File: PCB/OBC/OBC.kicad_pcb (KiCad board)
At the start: 4 copper layers, 81 x 81 mm, 130 parts, among them IC1 TPS2553QDBVRQ1, J2 Conn_02x24_Odd_Even, J3 USB_C_Receptacle_USB2.0_16P, U1 STM32F405RGTx, U10 TMUX1574PWR, U11 W25Q128JVSIQ, U12 SN65HVD230DR, U2 SN65HVD230DR, U3 USBLC6-2SC6, U4 STM32F405RGTx, U5 STM32F405RGTx, U6 MAX6369KA+T, U7 AMS1117-3.3, U8 TMUX1574PWR, U9 W25Q128JVSIQ

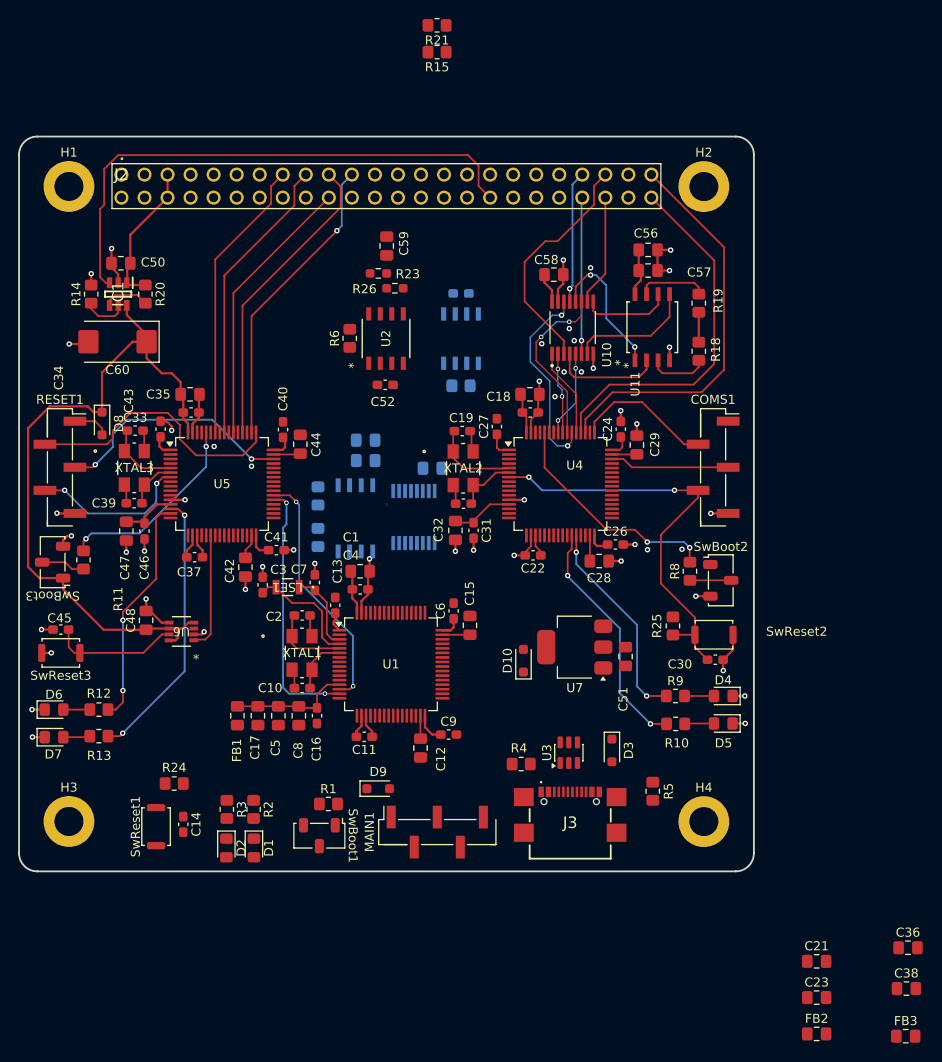
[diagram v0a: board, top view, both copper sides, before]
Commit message: Solo falta verificar el LDO
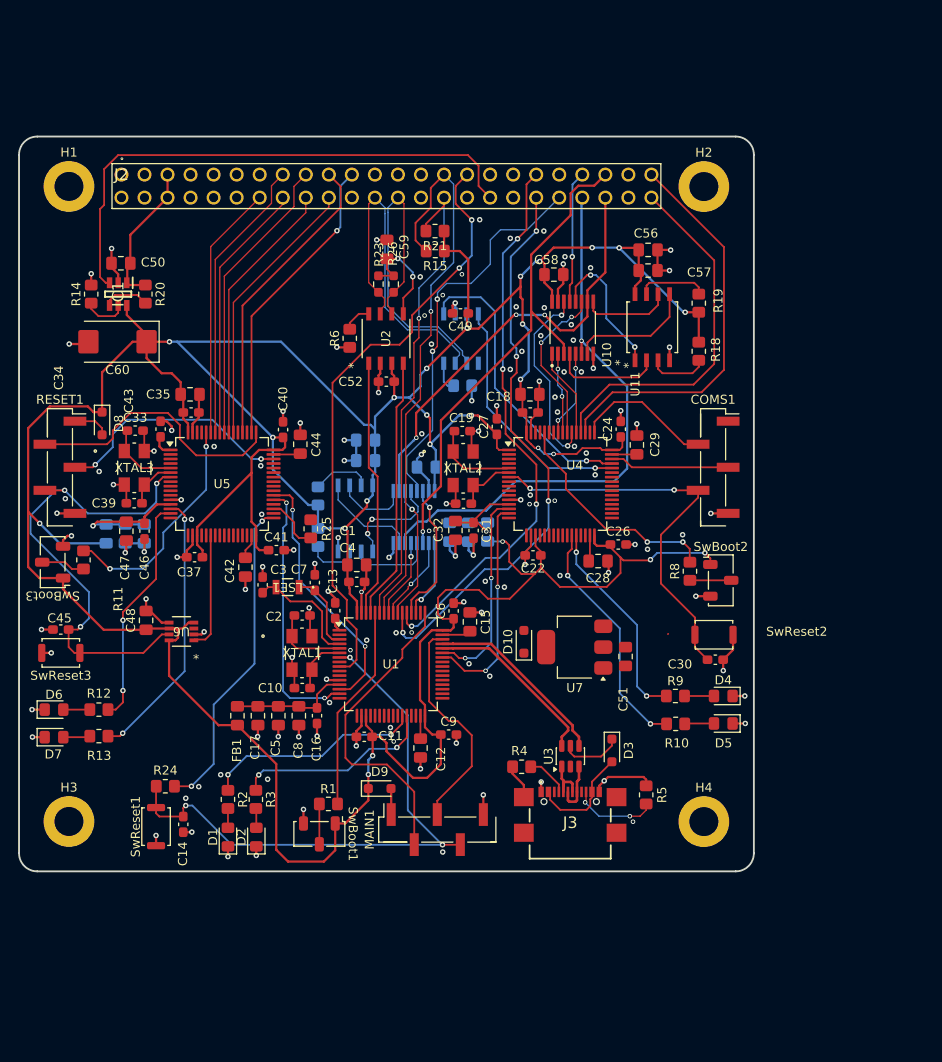
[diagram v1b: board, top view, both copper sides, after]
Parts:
- C21, C23, C36, C38, FB2, FB3: moved to B.Cu
- C49: moved to F.Cu
- moved FB3 104.1 mm to (119.5, 87.9), turned to 90 degrees
- moved C38 99.6 mm to (121.6, 87.9), turned to 90 degrees
- moved C36 95.8 mm to (123.7, 87.9), turned to 90 degrees
- moved FB2 66.2 mm to (161.6, 87.7), turned to 90 degrees
- moved C23 65.3 mm to (157.4, 87.7), turned to 90 degrees
- moved C21 60.9 mm to (159.4, 87.7), turned to 90 degrees
- moved R25 41.3 mm to (142.1, 87.3), turned to -90 degrees
- moved R21 22.7 mm to (155.8, 54.5)
- moved R15 21.9 mm to (155.8, 56.7)
- moved D2 3.51 mm to (136.1, 121.3), turned to 90 degrees
- moved R3 3.38 mm to (136.0, 117.2)
- moved D1 3.11 mm to (132.9, 121.3), turned to 90 degrees
- moved R2 3.03 mm to (132.9, 117.2)
- moved C49 2.20 mm to (158.6, 63.6)
- moved D10 2.09 mm to (165.6, 99.8)
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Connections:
- net CAN_H renamed CAN+
- net CAN_L renamed CAN-
- C16 pad 1: +3V3A -> +3V3AM
- C17 pad 1: +3V3A -> +3V3AM
- C21 pad 2: +3V3A -> +3V3AC
- C23 pad 2: +3V3A -> +3V3AC
- C31 pad 1: +3V3A -> +3V3AC
- C32 pad 1: +3V3A -> +3V3AC
- C36 pad 2: +3V3A -> +3V3AP
- C38 pad 2: +3V3A -> +3V3AP
- C46 pad 1: +3V3A -> +3V3AP
- C47 pad 1: +3V3A -> +3V3AP
- C5 pad 2: +3V3A -> +3V3AM
- C8 pad 2: +3V3A -> +3V3AM
- FB1 pad 2: +3V3A -> +3V3AM
- FB2 pad 2: +3V3A -> +3V3AC
- FB3 pad 2: +3V3A -> +3V3AP
- U1 pad 13: +3V3A -> +3V3AM
- U1 pad 37: SW2 -> unconnected-(U1-PC6-Pad37)
- U1 pad 38: SW1 -> unconnected-(U1-PC7-Pad38)
- U1 pad 40: EN_QUEMADOR -> unconnected-(U1-PC9-Pad40)
- U1 pad 50: CsMemPY -> unconnected-(U1-PA15-Pad50)
- U4 pad 13: +3V3A -> +3V3AC
- U5 pad 13: +3V3A -> +3V3AP
- U5 pad 55: unconnected-(U5-PB3-Pad55) -> EN_QUEMADOR
- U5 pad 57: unconnected-(U5-PB5-Pad57) -> SW2
- U5 pad 59: unconnected-(U5-PB7-Pad59) -> SW1
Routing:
- net +3V3: track 130.6 -> 484.3 mm, vias 0 -> 25
- net GND: track 105.4 -> 179.9 mm, vias 39 -> 133
- net Interrupción EPS: track 0.00 -> 66.3 mm, vias 0 -> 2
- net /Main/SWNRST: track 0.00 -> 65.6 mm, vias 0 -> 3
- net PY2_RX: track 0.00 -> 63.5 mm, vias 0 -> 4
- net I2C_SCL: track 0.00 -> 62.1 mm, vias 0 -> 1
- net PY2_TX: track 0.00 -> 61.6 mm, vias 0 -> 4
- net I2C_SDA: track 0.00 -> 53.2 mm, vias 0 -> 1
- net SPI_MOSI: track 17.2 -> 61.8 mm
- net CS_PY2: track 0.00 -> 43.1 mm, vias 0 -> 2
- net CAN-: track 0.00 -> 38.3 mm, vias 1 -> 0
- net CAN+: track 0.00 -> 38.2 mm
- net SPI_SCK: track 12.3 -> 48.0 mm, vias 0 -> 3
- net MainRst: track 0.00 -> 35.7 mm, vias 0 -> 2
- net /Main/SWCLK: track 0.00 -> 34.6 mm
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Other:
- outline, holes or cut-outs redrawn

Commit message: Routing finished, without errors
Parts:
- added C61: 10uF, Capacitor_SMD:C_0805_2012Metric_Pad1.18x1.45mm_HandSolder, F.Cu at (165.8, 99.3)
- R25: moved to B.Cu
- moved D10 14.1 mm to (179.7, 100.0), turned to -90 degrees
- moved R25 13.8 mm to (133.0, 97.8), turned to 90 degrees
- moved C51 8.98 mm to (168.0, 99.3), turned to 90 degrees
- moved U7 3.06 mm to (174.1, 99.4), turned to 0 degrees
- moved D8 0.23 mm to (119.0, 75.5)
- moved C35 0.12 mm to (128.9, 74.4)
- moved R17 0.10 mm to (142.9, 83.7)
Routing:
- net /Coms/SWNRST_Com: track 44.1 -> 147.4 mm, vias 2 -> 3
- net d3v3: track 2.88 -> 96.9 mm
- net +3V3: track 484.3 -> 512.2 mm, vias 25 -> 27
- net Net-(D10-A): track 0.00 -> 15.0 mm
- net +5V: track 6.72 -> 17.2 mm
- net ComsRst: track 6.11 -> 15.4 mm, vias 0 -> 1
- net +Vbatt: track 15.9 -> 22.6 mm
- net GND: track 179.9 -> 185.5 mm, vias 133 -> 150
- net 5V: track 0.00 -> 2.54 mm
- net Net-(D3-A): track 11.9 -> 12.7 mm

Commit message: Skillsreen
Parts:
- moved C13 0.60 mm to (144.7, 95.8)
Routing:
- net +3V3: track 512.2 -> 513.0 mm
- net GND: track 185.5 -> 186.2 mm
